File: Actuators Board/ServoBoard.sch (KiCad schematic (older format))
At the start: 45 parts, among them J10 Conn_01x02_Male, J9 Conn_01x02_Male, Q1 MMDT2222A

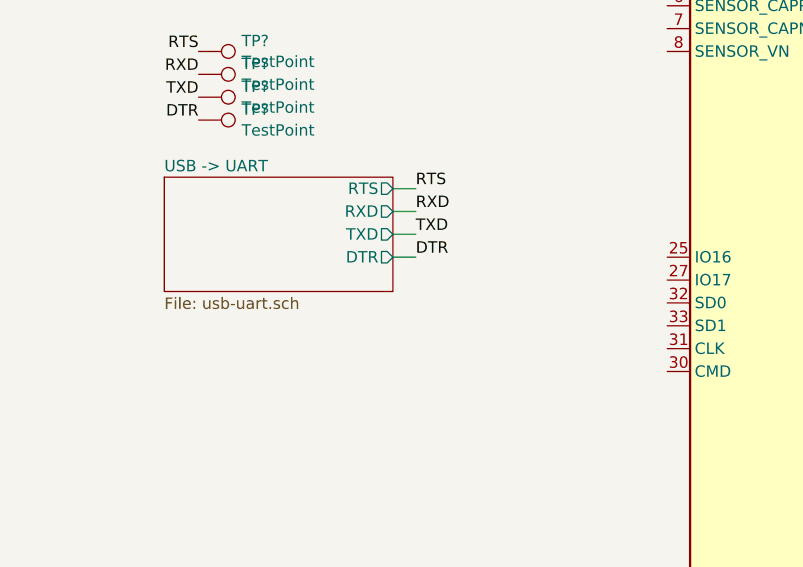
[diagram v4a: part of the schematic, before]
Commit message: Connected 3.3V output from USB-UART converter
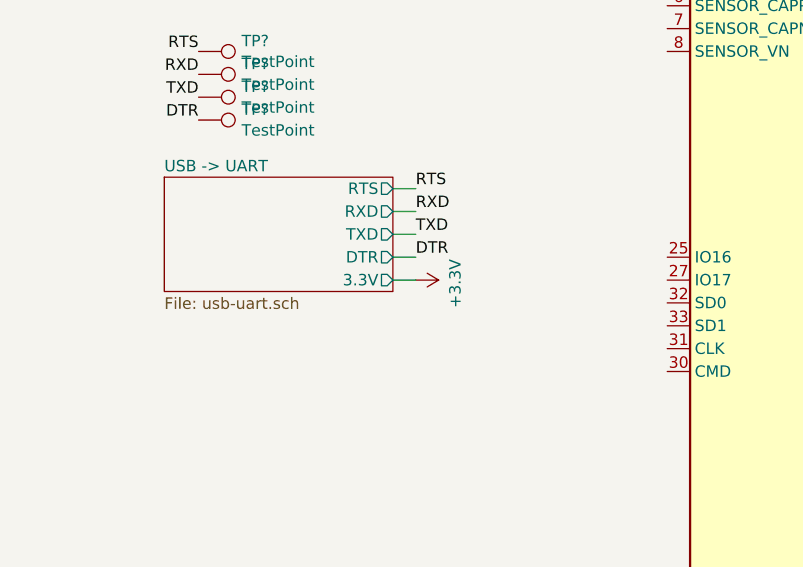
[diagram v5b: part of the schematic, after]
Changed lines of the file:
@@
 F4 "TXD" O R 2200 3450 50
 F5 "DTR" O R 2200 3550 50
+F6 "3.3V" O R 2200 3650 50
 $EndSheet
 $Comp
@@
 Connection ~ 3700 1800
 Connection ~ 4000 1900
+Wire Wire Line
+	2200 3650 2300 3650
+$Comp
+L power:+3.3V #PWR?
+U 1 1 61A7095B
+P 2300 3650
+AR Path="/61A7095B" Ref="#PWR?"  Part="1"
+AR Path="/61AA560B/61A7095B" Ref="#PWR?"  Part="1"
+F 0 "#PWR?" H 2300 3500 50  0001 C CNN
+F 1 "+3.3V" H 2315 3823 50  0000 C CNN
+F 2 "" H 2300 3650 50  0001 C CNN
+F 3 "" H 2300 3650 50  0001 C CNN
+	1    2300 3650
+	0    1    1    0
+$EndComp
 $EndSCHEMATC

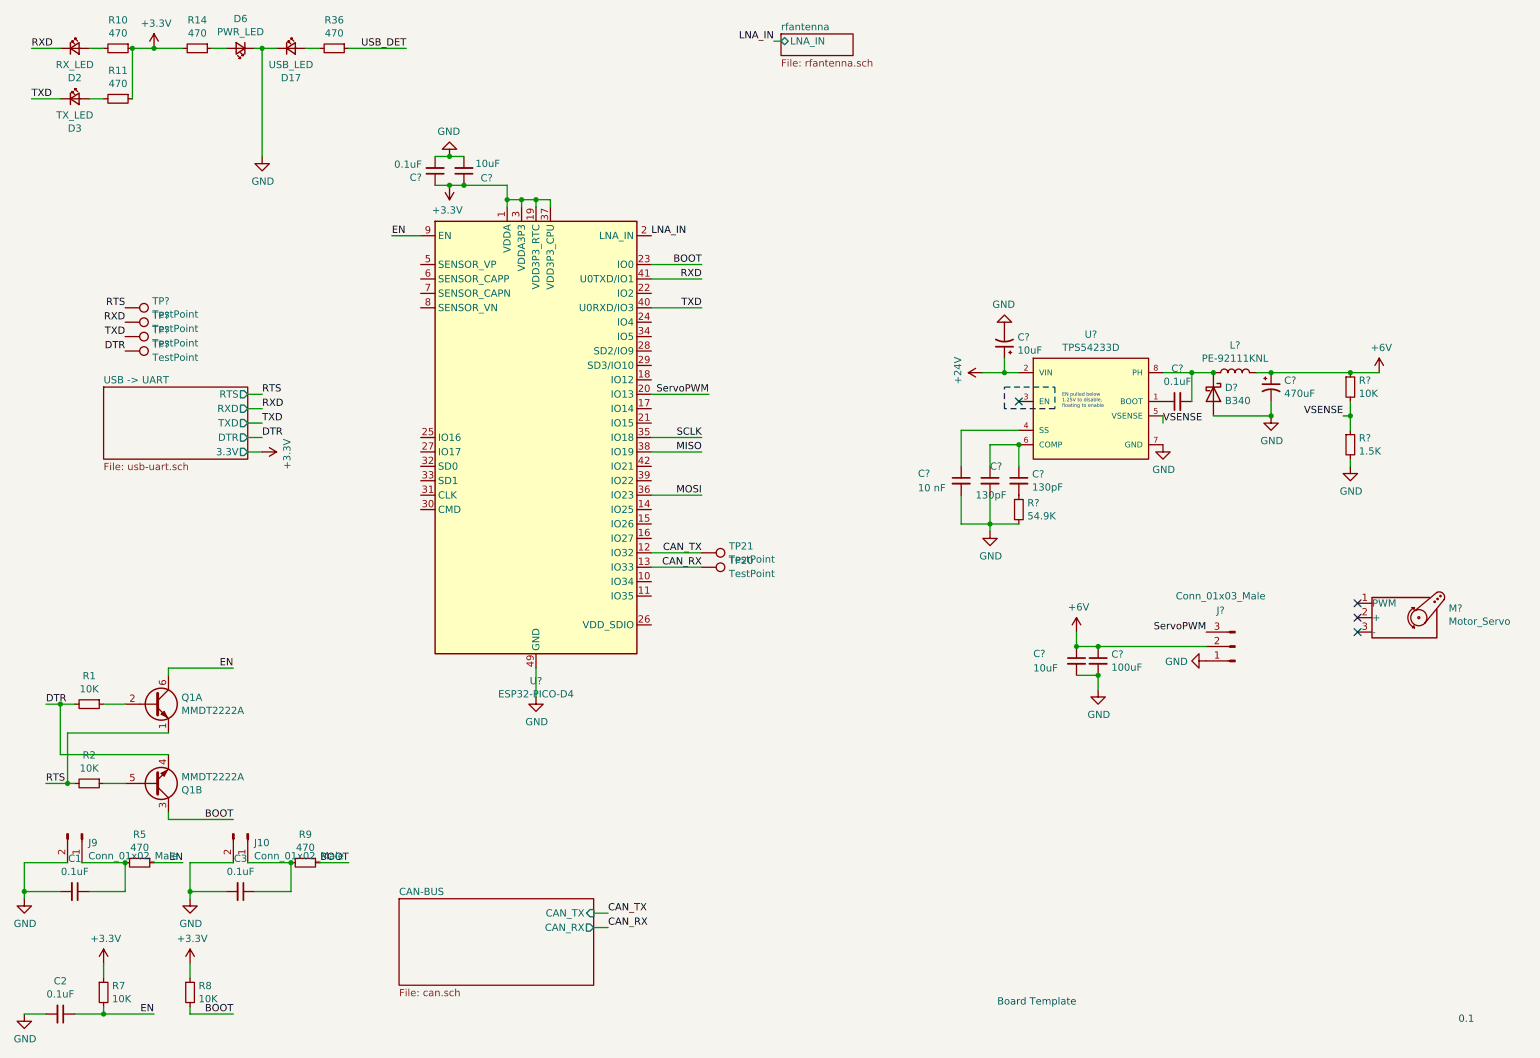
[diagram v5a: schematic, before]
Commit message: added test points on servo board
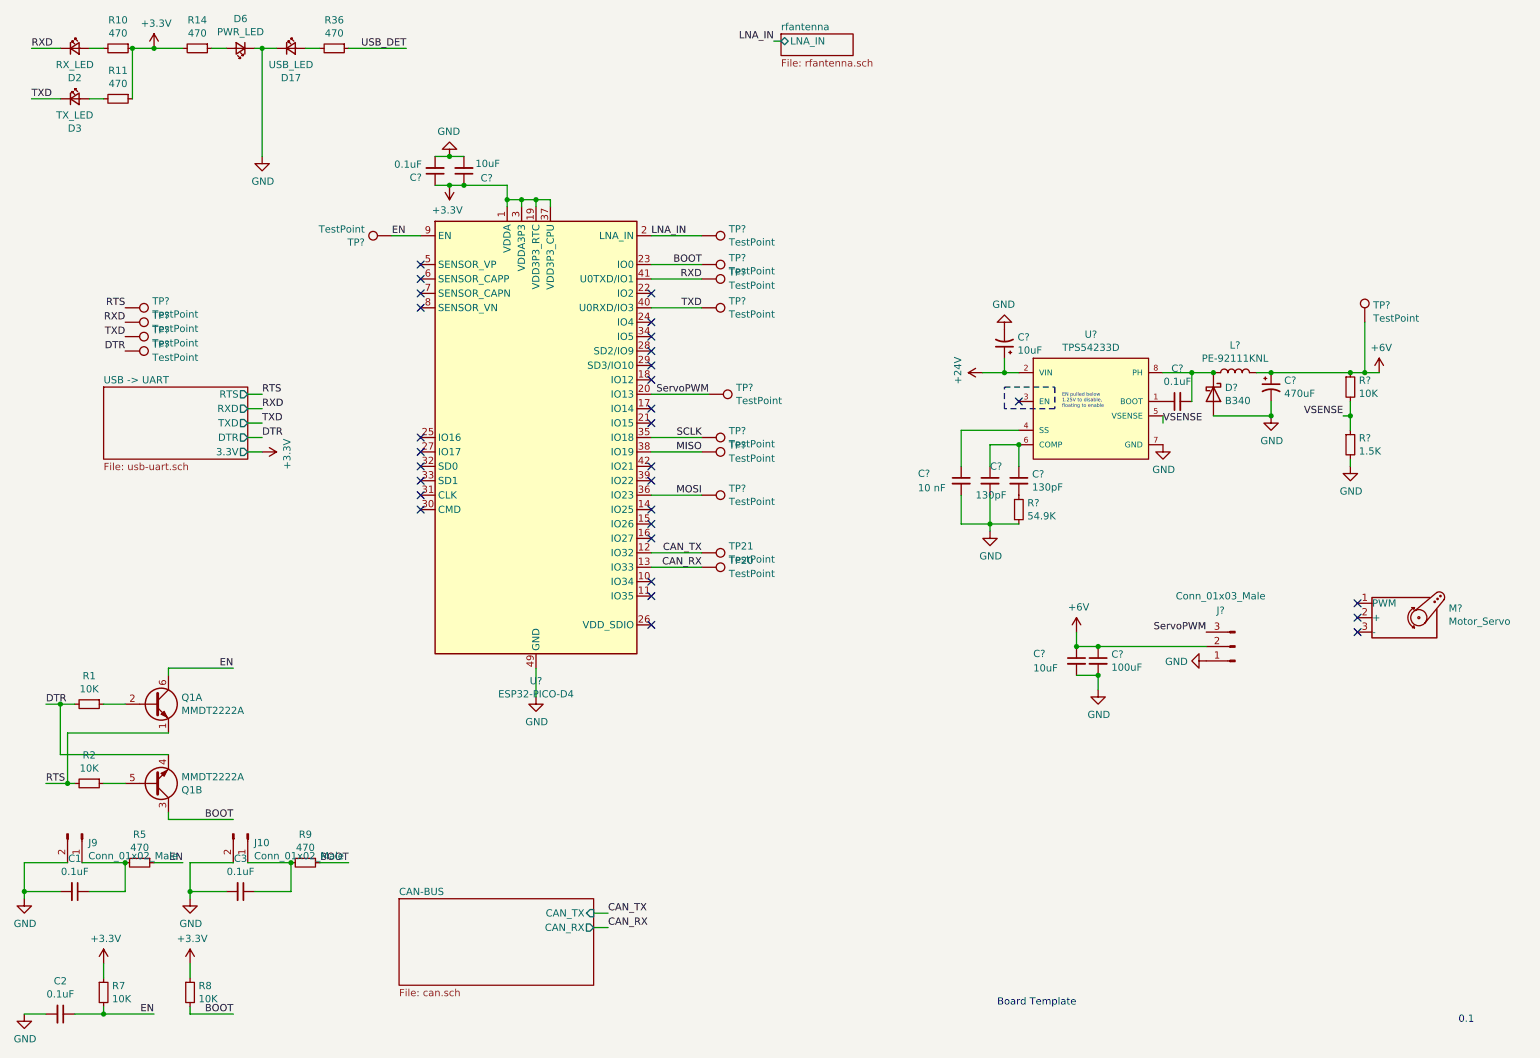
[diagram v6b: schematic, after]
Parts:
- added TP? (x10): TestPoint, symbol Connector:TestPoint
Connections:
- net +6V: now also TP?.1
- net BOOT: now also TP?.1
- net EN: now also TP?.1
- net LNA_IN: now also TP?.1
- net MISO: now also TP?.1
- net MOSI: now also TP?.1
- net RXD: now also TP?.1
- net SCLK: now also TP?.1
- net ServoPWM: now also TP?.1
- net TXD: now also TP?.1
- no-connect marks 4 -> 30
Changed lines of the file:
@@
 	7350 4150 7350 4200
 Wire Wire Line
-	9850 3100 10050 3100
+	9850 3100 9950 3100
 Connection ~ 9850 3100
 $Comp
@@
 	0    1    1    0
 $EndComp
+$Comp
+L Connector:TestPoint TP?
+U 1 1 61AFEC97
+P 5350 3950
+F 0 "TP?" V 5304 4138 50  0000 L CNN
+F 1 "TestPoint" V 5395 4138 50  0000 L CNN
+F 2 "" H 5550 3950 50  0001 C CNN
+F 3 "~" H 5550 3950 50  0001 C CNN
+	1    5350 3950
+	0    1    1    0
+$EndComp
+$Comp
+L Connector:TestPoint TP?
+U 1 1 61AFFB17
+P 5350 3650
+F 0 "TP?" V 5304 3838 50  0000 L CNN
+F 1 "TestPoint" V 5395 3838 50  0000 L CNN
+F 2 "" H 5550 3650 50  0001 C CNN
+F 3 "~" H 5550 3650 50  0001 C CNN
+	1    5350 3650
+	0    1    1    0
+$EndComp
+$Comp
+L Connector:TestPoint TP?
+U 1 1 61B06C77
+P 5350 3550
+F 0 "TP?" V 5304 3738 50  0000 L CNN
+F 1 "TestPoint" V 5395 3738 50  0000 L CNN
+F 2 "" H 5550 3550 50  0001 C CNN
+F 3 "~" H 5550 3550 50  0001 C CNN
+	1    5350 3550
+	0    1    1    0
+$EndComp
+$Comp
+L Connector:TestPoint TP?
+U 1 1 61B0E262
+P 5400 3250
+F 0 "TP?" V 5354 3438 50  0000 L CNN
+F 1 "TestPoint" V 5445 3438 50  0000 L CNN
+F 2 "" H 5600 3250 50  0001 C CNN
+F 3 "~" H 5600 3250 50  0001 C CNN
+	1    5400 3250
+	0    1    1    0
+$EndComp
+$Comp
+L Connector:TestPoint TP?
+U 1 1 61B11A26
+P 5350 2650
+F 0 "TP?" V 5304 2838 50  0000 L CNN
+F 1 "TestPoint" V 5395 2838 50  0000 L CNN
+F 2 "" H 5550 2650 50  0001 C CNN
+F 3 "~" H 5550 2650 50  0001 C CNN
+	1    5350 2650
+	0    1    1    0
+$EndComp
+$Comp
+L Connector:TestPoint TP?
+U 1 1 61B19901
+P 5350 2450
+F 0 "TP?" V 5304 2638 50  0000 L CNN
+F 1 "TestPoint" V 5395 2638 50  0000 L CNN
+F 2 "" H 5550 2450 50  0001 C CNN
+F 3 "~" H 5550 2450 50  0001 C CNN
+	1    5350 2450
+	0    1    1    0
+$EndComp
+$Comp
+L Connector:TestPoint TP?
+U 1 1 61B1D3C4
+P 5350 2350
+F 0 "TP?" V 5304 2538 50  0000 L CNN
+F 1 "TestPoint" V 5395 2538 50  0000 L CNN
+F 2 "" H 5550 2350 50  0001 C CNN
+F 3 "~" H 5550 2350 50  0001 C CNN
+	1    5350 2350
+	0    1    1    0
+$EndComp
+$Comp
+L Connector:TestPoint TP?
+U 1 1 61B216B6
+P 3200 2150
+F 0 "TP?" V 3154 2338 50  0000 L CNN
+F 1 "TestPoint" V 3245 2338 50  0000 L CNN
+F 2 "" H 3400 2150 50  0001 C CNN
+F 3 "~" H 3400 2150 50  0001 C CNN
+	1    3200 2150
+	0    -1   -1   0
+$EndComp
+$Comp
+L Connector:TestPoint TP?
+U 1 1 61B25948
+P 5350 2150
+F 0 "TP?" V 5304 2338 50  0000 L CNN
+F 1 "TestPoint" V 5395 2338 50  0000 L CNN
+F 2 "" H 5550 2150 50  0001 C CNN
+F 3 "~" H 5550 2150 50  0001 C CNN
+	1    5350 2150
+	0    1    1    0
+$EndComp
+Wire Wire Line
+	5350 2150 5000 2150
+NoConn ~ 5000 2550
+NoConn ~ 5000 2750
+NoConn ~ 5000 2850
+NoConn ~ 5000 2950
+NoConn ~ 5000 3050
+NoConn ~ 5000 3150
+NoConn ~ 5000 3350
+NoConn ~ 5000 3450
+NoConn ~ 5000 3750
+NoConn ~ 5000 3850
+NoConn ~ 5000 4050
+NoConn ~ 5000 4150
+NoConn ~ 5000 4250
+NoConn ~ 5000 4550
+NoConn ~ 5000 4650
+NoConn ~ 5000 4850
+NoConn ~ 3400 4050
+NoConn ~ 3400 3950
+NoConn ~ 3400 3850
+NoConn ~ 3400 3750
+NoConn ~ 3400 3650
+NoConn ~ 3400 3550
+NoConn ~ 3400 2650
+NoConn ~ 3400 2550
+NoConn ~ 3400 2450
+NoConn ~ 3400 2350
+$Comp
+L Connector:TestPoint TP?
+U 1 1 61B8F221
+P 9950 2750
+F 0 "TP?" H 10008 2868 50  0000 L CNN
+F 1 "TestPoint" H 10008 2777 50  0000 L CNN
+F 2 "" H 10150 2750 50  0001 C CNN
+F 3 "~" H 10150 2750 50  0001 C CNN
+	1    9950 2750
+	1    0    0    -1
+$EndComp
+Wire Wire Line
+	9950 2750 9950 3100
+Connection ~ 9950 3100
+Wire Wire Line
+	9950 3100 10050 3100
 $EndSCHEMATC

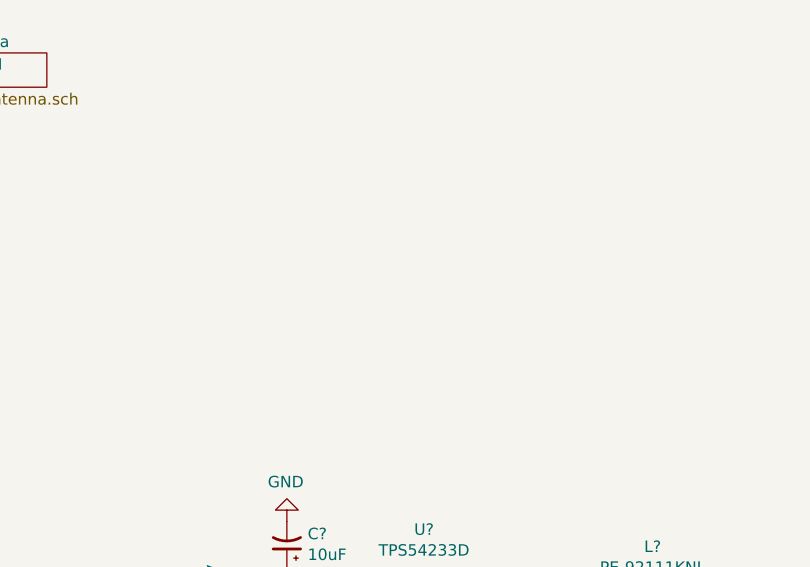
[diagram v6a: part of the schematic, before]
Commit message: power connectors (servo)
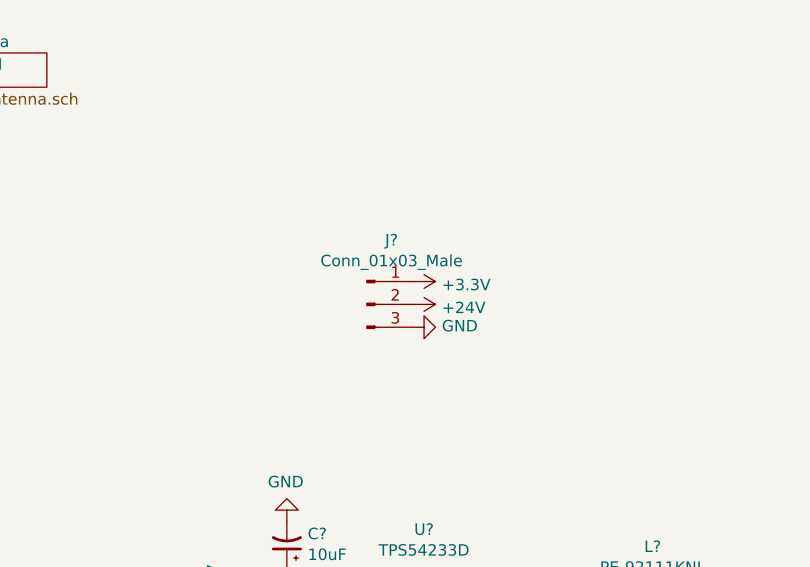
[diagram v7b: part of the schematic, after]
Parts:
- added J?: Conn_01x03_Male, symbol Connector:Conn_01x03_Male
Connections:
- net +24V: now also J?.2 (Pin_2)
- net +3V3: now also J?.1 (Pin_1)
- net GND: now also J?.3 (Pin_3)
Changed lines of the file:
@@
 Wire Wire Line
 	9950 3100 10050 3100
+$Comp
+L Connector:Conn_01x03_Male J?
+U 1 1 61AFFBA8
+P 7800 1850
+F 0 "J?" H 7908 2131 50  0000 C CNN
+F 1 "Conn_01x03_Male" H 7908 2040 50  0000 C CNN
+F 2 "" H 7800 1850 50  0001 C CNN
+F 3 "~" H 7800 1850 50  0001 C CNN
+	1    7800 1850
+	1    0    0    -1
+$EndComp
+$Comp
+L power:+3.3V #PWR?
+U 1 1 61B008BE
+P 8000 1750
+F 0 "#PWR?" H 8000 1600 50  0001 C CNN
+F 1 "+3.3V" V 8015 1878 50  0000 L CNN
+F 2 "" H 8000 1750 50  0001 C CNN
+F 3 "" H 8000 1750 50  0001 C CNN
+	1    8000 1750
+	0    1    1    0
+$EndComp
+$Comp
+L power:+24V #PWR?
+U 1 1 61B017E5
+P 8000 1850
+F 0 "#PWR?" H 8000 1700 50  0001 C CNN
+F 1 "+24V" V 8015 1978 50  0000 L CNN
+F 2 "" H 8000 1850 50  0001 C CNN
+F 3 "" H 8000 1850 50  0001 C CNN
+	1    8000 1850
+	0    1    1    0
+$EndComp
+$Comp
+L power:GND #PWR?
+U 1 1 61B02595
+P 8000 1950
+F 0 "#PWR?" H 8000 1700 50  0001 C CNN
+F 1 "GND" V 8005 1822 50  0000 R CNN
+F 2 "" H 8000 1950 50  0001 C CNN
+F 3 "" H 8000 1950 50  0001 C CNN
+	1    8000 1950
+	0    -1   -1   0
+$EndComp
 $EndSCHEMATC

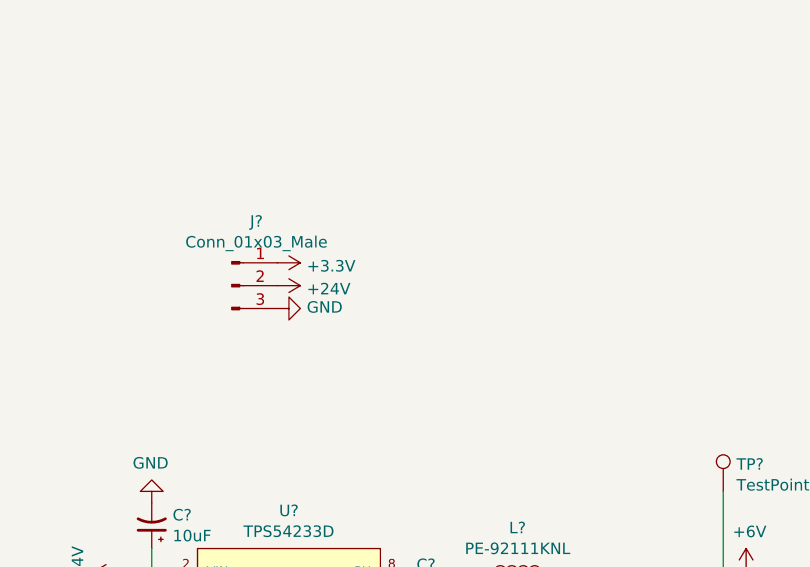
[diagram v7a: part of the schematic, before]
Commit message: Fixed power connections (servo)
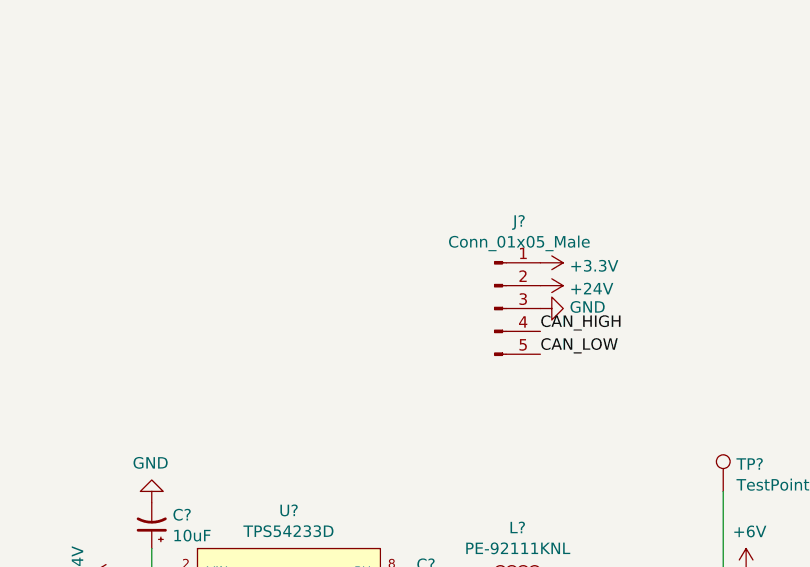
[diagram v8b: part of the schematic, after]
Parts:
- removed J?: Conn_01x03_Male, symbol Connector:Conn_01x03_Male
- added J?: Conn_01x05_Male, symbol Connector:Conn_01x05_Male
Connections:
- net +24V: now also J?.2 (Pin_2)
- net +3V3: now also J?.1 (Pin_1)
- net GND: now also J?.3 (Pin_3)
- new net CAN_HIGH: J?.4 (Pin_4)
- new net CAN_LOW: J?.5 (Pin_5)
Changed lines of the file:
@@
 	9950 3100 10050 3100
-$Comp
-L Connector:Conn_01x03_Male J?
-U 1 1 61AFFBA8
-P 7800 1850
-F 0 "J?" H 7908 2131 50  0000 C CNN
-F 1 "Conn_01x03_Male" H 7908 2040 50  0000 C CNN
-F 2 "" H 7800 1850 50  0001 C CNN
-F 3 "~" H 7800 1850 50  0001 C CNN
-	1    7800 1850
-	1    0    0    -1
-$EndComp
 $Comp
 L power:+3.3V #PWR?
 U 1 1 61B008BE
-P 8000 1750
-F 0 "#PWR?" H 8000 1600 50  0001 C CNN
-F 1 "+3.3V" V 8015 1878 50  0000 L CNN
-F 2 "" H 8000 1750 50  0001 C CNN
-F 3 "" H 8000 1750 50  0001 C CNN
-	1    8000 1750
+P 9150 1750
+F 0 "#PWR?" H 9150 1600 50  0001 C CNN
+F 1 "+3.3V" V 9165 1878 50  0000 L CNN
+F 2 "" H 9150 1750 50  0001 C CNN
+F 3 "" H 9150 1750 50  0001 C CNN
+	1    9150 1750
 	0    1    1    0
 $EndComp
@@
 L power:+24V #PWR?
 U 1 1 61B017E5
-P 8000 1850
-F 0 "#PWR?" H 8000 1700 50  0001 C CNN
-F 1 "+24V" V 8015 1978 50  0000 L CNN
-F 2 "" H 8000 1850 50  0001 C CNN
-F 3 "" H 8000 1850 50  0001 C CNN
-	1    8000 1850
+P 9150 1850
+F 0 "#PWR?" H 9150 1700 50  0001 C CNN
+F 1 "+24V" V 9165 1978 50  0000 L CNN
+F 2 "" H 9150 1850 50  0001 C CNN
+F 3 "" H 9150 1850 50  0001 C CNN
+	1    9150 1850
 	0    1    1    0
 $EndComp
@@
 L power:GND #PWR?
 U 1 1 61B02595
-P 8000 1950
-F 0 "#PWR?" H 8000 1700 50  0001 C CNN
-F 1 "GND" V 8005 1822 50  0000 R CNN
-F 2 "" H 8000 1950 50  0001 C CNN
-F 3 "" H 8000 1950 50  0001 C CNN
-	1    8000 1950
+P 9150 1950
+F 0 "#PWR?" H 9150 1700 50  0001 C CNN
+F 1 "GND" V 9155 1822 50  0000 R CNN
+F 2 "" H 9150 1950 50  0001 C CNN
+F 3 "" H 9150 1950 50  0001 C CNN
+	1    9150 1950
 	0    -1   -1   0
 $EndComp
+$Comp
+L Connector:Conn_01x05_Male J?
+U 1 1 61B03907
+P 8950 1950
+F 0 "J?" H 9058 2331 50  0000 C CNN
+F 1 "Conn_01x05_Male" H 9058 2240 50  0000 C CNN
+F 2 "" H 8950 1950 50  0001 C CNN
+F 3 "~" H 8950 1950 50  0001 C CNN
+	1    8950 1950
+	1    0    0    -1
+$EndComp
+Text Label 9150 2050 0    50   ~ 0
+CAN_HIGH
+Text Label 9150 2150 0    50   ~ 0
+CAN_LOW
 $EndSCHEMATC
